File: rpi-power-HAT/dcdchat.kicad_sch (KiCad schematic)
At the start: 28 parts

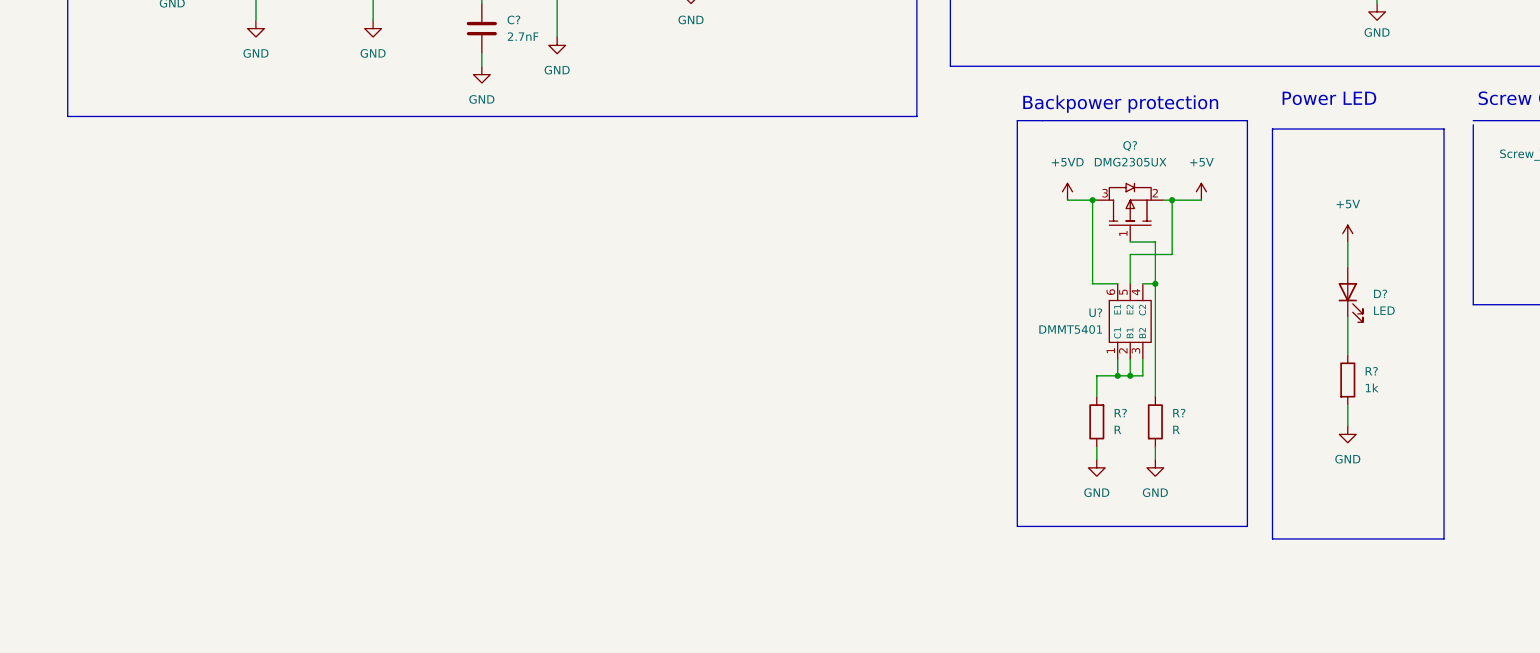
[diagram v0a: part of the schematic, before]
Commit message: added gpio connector
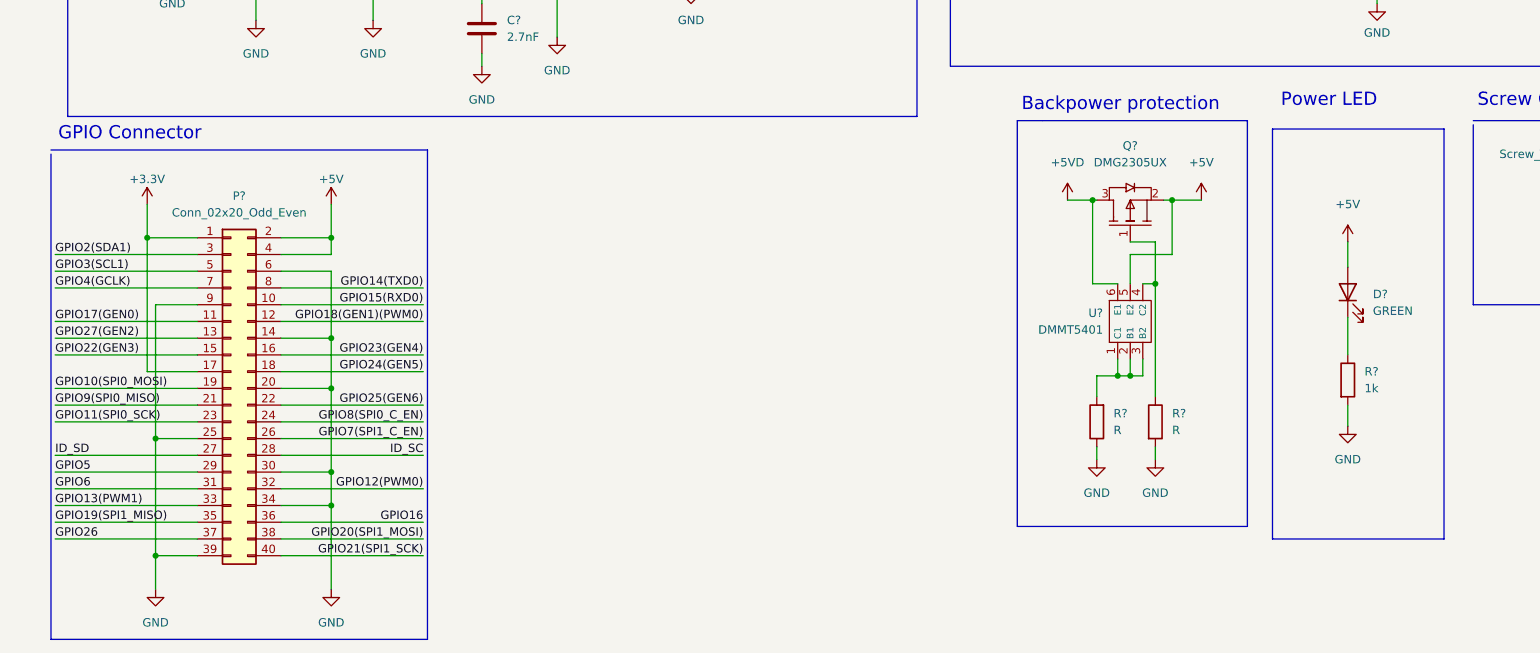
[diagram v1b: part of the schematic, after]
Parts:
- added P?: Conn_02x20_Odd_Even, Connector_PinSocket_2.54mm:PinSocket_2x20_P2.54mm_Vertical, symbol Library:Conn_02x20_Odd_Even
- D?: value LED -> GREEN
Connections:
- net +3.3V: now also P?.1 (Pin_1), P?.17 (Pin_17)
- net +5V: now also P?.2 (Pin_2), P?.4 (Pin_4)
- net GND: now also P?.14 (Pin_14), P?.20 (Pin_20), P?.25 (Pin_25), P?.30 (Pin_30), P?.34 (Pin_34), P?.39 (Pin_39), P?.6 (Pin_6), P?.9 (Pin_9)
- new net GPIO10(SPI0_MOSI): P?.19 (Pin_19)
- new net GPIO11(SPI0_SCK): P?.23 (Pin_23)
- new net GPIO12(PWM0): P?.32 (Pin_32)
- new net GPIO13(PWM1): P?.33 (Pin_33)
- new net GPIO14(TXD0): P?.8 (Pin_8)
- new net GPIO15(RXD0): P?.10 (Pin_10)
- new net GPIO16: P?.36 (Pin_36)
- new net GPIO17(GEN0): P?.11 (Pin_11)
- new net GPIO18(GEN1)(PWM0): P?.12 (Pin_12)
- new net GPIO19(SPI1_MISO): P?.35 (Pin_35)
- new net GPIO2(SDA1): P?.3 (Pin_3)
- new net GPIO20(SPI1_MOSI): P?.38 (Pin_38)
- new net GPIO21(SPI1_SCK): P?.40 (Pin_40)
- new net GPIO22(GEN3): P?.15 (Pin_15)
- new net GPIO23(GEN4): P?.16 (Pin_16)
- new net GPIO24(GEN5): P?.18 (Pin_18)
- new net GPIO25(GEN6): P?.22 (Pin_22)
- new net GPIO26: P?.37 (Pin_37)
- new net GPIO27(GEN2): P?.13 (Pin_13)
- new net GPIO3(SCL1): P?.5 (Pin_5)
- new net GPIO4(GCLK): P?.7 (Pin_7)
- new net GPIO5: P?.29 (Pin_29)
- new net GPIO6: P?.31 (Pin_31)
- new net GPIO7(SPI1_C_EN): P?.26 (Pin_26)
- new net GPIO8(SPI0_C_EN): P?.24 (Pin_24)
- new net GPIO9(SPI0_MISO): P?.21 (Pin_21)
- new net ID_SC: P?.28 (Pin_28)
- new net ID_SD: P?.27 (Pin_27)
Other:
- note added: "GPIO Connector"

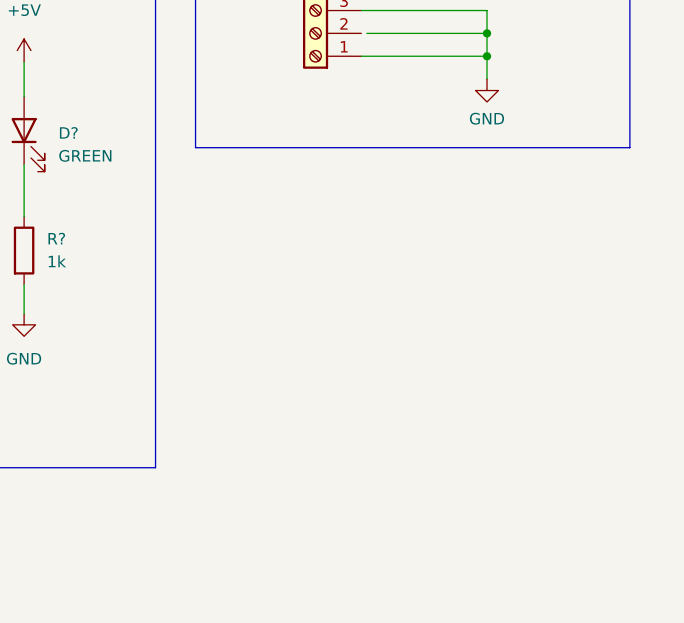
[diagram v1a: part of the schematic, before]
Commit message: Added readme, added CHassis connector
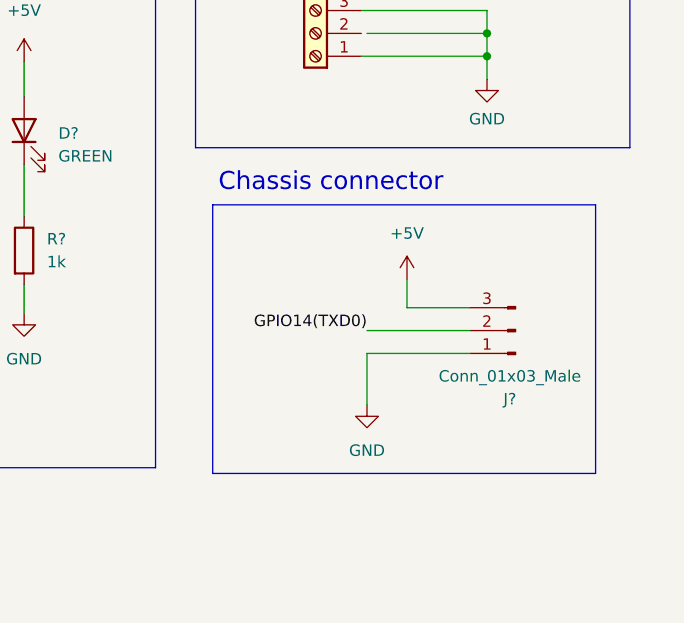
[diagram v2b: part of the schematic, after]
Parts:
- added J?: Conn_01x03_Male, symbol Connector:Conn_01x03_Male
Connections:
- net +5V: now also J?.3 (Pin_3)
- net GND: now also J?.1 (Pin_1)
- net GPIO14(TXD0): now also J?.2 (Pin_2)
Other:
- note added: "Chassis connector"
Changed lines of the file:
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@@
+    (stroke (width 0) (type default) (color 0 0 0 0))
+  )
+  (wire (pts (xy 248.92 131.445) (xy 260.35 131.445))
     (stroke (width 0) (type default) (color 0 0 0 0))
   )
@@
     (stroke (width 0) (type default) (color 0 0 0 0))
   )
+  (polyline (pts (xy 231.775 117.475) (xy 231.775 147.32))
+    (stroke (width 0) (type default) (color 0 0 0 0))
+  )
   (wire (pts (xy 215.265 36.83) (xy 215.265 40.005))
     (stroke (width 0) (type default) (color 0 0 0 0))
@@
     (stroke (width 0) (type default) (color 0 0 0 0))
   )
+  (polyline (pts (xy 231.775 117.475) (xy 274.32 117.475))
+    (stroke (width 0) (type default) (color 0 0 0 0))
+  )
   (wire (pts (xy 248.92 98.425) (xy 262.255 98.425))
     (stroke (width 0) (type default) (color 0 0 0 0))
@@
     (stroke (width 0) (type default) (color 0 0 0 0))
   )
+  (wire (pts (xy 253.365 125.73) (xy 253.365 128.905))
+    (stroke (width 0) (type default) (color 0 0 0 0))
+  )
   (polyline (pts (xy 150.495 17.145) (xy 150.495 74.93))
     (stroke (width 0) (type default) (color 0 0 0 0))
@@
     (stroke (width 0) (type default) (color 0 0 0 0))
   )
+  (polyline (pts (xy 274.32 117.475) (xy 274.32 147.32))
+    (stroke (width 0) (type default) (color 0 0 0 0))
+  )
   (wire (pts (xy 51.435 52.705) (xy 45.085 52.705))
     (stroke (width 0) (type default) (color 0 0 0 0))
@@
     (stroke (width 0) (type default) (color 0 0 0 0))
   )
+  (polyline (pts (xy 274.32 147.32) (xy 231.775 147.32))
+    (stroke (width 0) (type default) (color 0 0 0 0))
+  )
   (wire (pts (xy 172.72 132.715) (xy 172.72 134.62))
     (stroke (width 0) (type default) (color 0 0 0 0))
@@
     (stroke (width 0) (type default) (color 0 0 0 0))
   )
+  (wire (pts (xy 260.35 128.905) (xy 253.365 128.905))
+    (stroke (width 0) (type default) (color 0 0 0 0))
+  )
   (wire (pts (xy 48.895 128.905) (xy 70.485 128.905))
     (stroke (width 0) (type default) (color 0 0 0 0))
@@
     (stroke (width 0) (type default) (color 0 0 0 0))
   )
+  (wire (pts (xy 260.35 133.985) (xy 248.92 133.985))
+    (stroke (width 0) (type default) (color 0 0 0 0))
+  )
   (wire (pts (xy 28.575 121.285) (xy 36.195 121.285))
     (stroke (width 0) (type default) (color 0 0 0 0))
@@
   )
   (polyline (pts (xy 195.58 83.185) (xy 195.58 144.78))
+    (stroke (width 0) (type default) (color 0 0 0 0))
+  )
+  (wire (pts (xy 248.92 133.985) (xy 248.92 139.7))
     (stroke (width 0) (type default) (color 0 0 0 0))
   )
@@
     (effects (font (size 2 2)) (justify left bottom))
   )
+  (text "Chassis connector" (at 232.41 116.205 0)
+    (effects (font (size 2 2)) (justify left bottom))
+  )
   (text "Power LED" (at 200.66 81.28 0)
     (effects (font (size 2 2)) (justify left bottom))
@@
   )
   (label "GPIO20(SPI1_MOSI)" (at 70.485 146.685 180)
+    (effects (font (size 1.27 1.27)) (justify right bottom))
+  )
+  (label "GPIO14(TXD0)" (at 248.92 131.445 180)
     (effects (font (size 1.27 1.27)) (justify right bottom))
   )
@@
     )
     (property "Datasheet" "" (id 3) (at 262.255 90.805 0)
+      (effects (font (size 1.27 1.27)) hide)
+    )
+    (pin "1")
+  )
+  (symbol (lib_id "power:GND") (at 248.92 139.7 0) (unit 1)
+    (in_bom yes) (on_board yes) (fields_autoplaced)
+    (property "Reference" "#PWR?" (id 0) (at 248.92 146.05 0)
+      (effects (font (size 1.27 1.27)) hide)
+    )
+    (property "Value" "GND" (id 1) (at 248.92 144.78 0))
+    (property "Footprint" "" (id 2) (at 248.92 139.7 0)
+      (effects (font (size 1.27 1.27)) hide)
+    )
+    (property "Datasheet" "" (id 3) (at 248.92 139.7 0)
       (effects (font (size 1.27 1.27)) hide)
     )
@@
     (pin "4")
     (pin "5")
+  )
+  (symbol (lib_id "Connector:Conn_01x03_Male") (at 265.43 131.445 180) (unit 1)
+    (in_bom yes) (on_board yes) (fields_autoplaced)
+    (property "Reference" "J?" (id 0) (at 264.795 139.065 0))
+    (property "Value" "Conn_01x03_Male" (id 1) (at 264.795 136.525 0))
+    (property "Footprint" "" (id 2) (at 265.43 131.445 0)
+      (effects (font (size 1.27 1.27)) hide)
+    )
+    (property "Datasheet" "~" (id 3) (at 265.43 131.445 0)
+      (effects (font (size 1.27 1.27)) hide)
+    )
+    (pin "1")
+    (pin "2")
+    (pin "3")
   )
   (symbol (lib_id "power:GND") (at 181.61 134.62 0) (unit 1)
@@
     (pin "1")
   )
+  (symbol (lib_id "power:+5V") (at 253.365 125.73 0) (unit 1)
+    (in_bom yes) (on_board yes) (fields_autoplaced)
+    (property "Reference" "#PWR?" (id 0) (at 253.365 129.54 0)
+      (effects (font (size 1.27 1.27)) hide)
+    )
+    (property "Value" "+5V" (id 1) (at 253.365 120.65 0))
+    (property "Footprint" "" (id 2) (at 253.365 125.73 0)
+      (effects (font (size 1.27 1.27)) hide)
+    )
+    (property "Datasheet" "" (id 3) (at 253.365 125.73 0)
+      (effects (font (size 1.27 1.27)) hide)
+    )
+    (pin "1")
+  )
   (symbol (lib_id "Device:R") (at 210.82 122.555 0) (unit 1)
     (in_bom yes) (on_board yes) (fields_autoplaced)
@@
       (reference "#PWR?") (unit 1) (value "VCC") (footprint "")
     )
+    (path "/1683b790-0de4-48f6-98f7-032bf4ffe128"
+      (reference "#PWR?") (unit 1) (value "GND") (footprint "")
+    )
     (path "/16c81207-e246-4f87-8952-3ebeb878f8cb"
       (reference "#PWR?") (unit 1) (value "GND") (footprint "")
@@
       (reference "#PWR?") (unit 1) (value "+5VD") (footprint "")
     )
+    (path "/dfc07625-ddae-4ee3-aa1d-cab8d3a957a5"
+      (reference "#PWR?") (unit 1) (value "+5V") (footprint "")
+    )
     (path "/e69f3ab5-0847-439a-88e5-85d6eccfddba"
       (reference "#PWR?") (unit 1) (value "GND") (footprint "")
@@
       (reference "J?") (unit 1) (value "Screw_Terminal_01x05") (footprint "")
     )
+    (path "/739f876b-99d3-497e-b99f-98cc80035177"
+      (reference "J?") (unit 1) (value "Conn_01x03_Male") (footprint "")
+    )
     (path "/3eb396dd-1ed2-4bf1-bdc4-46cd0052b75b"

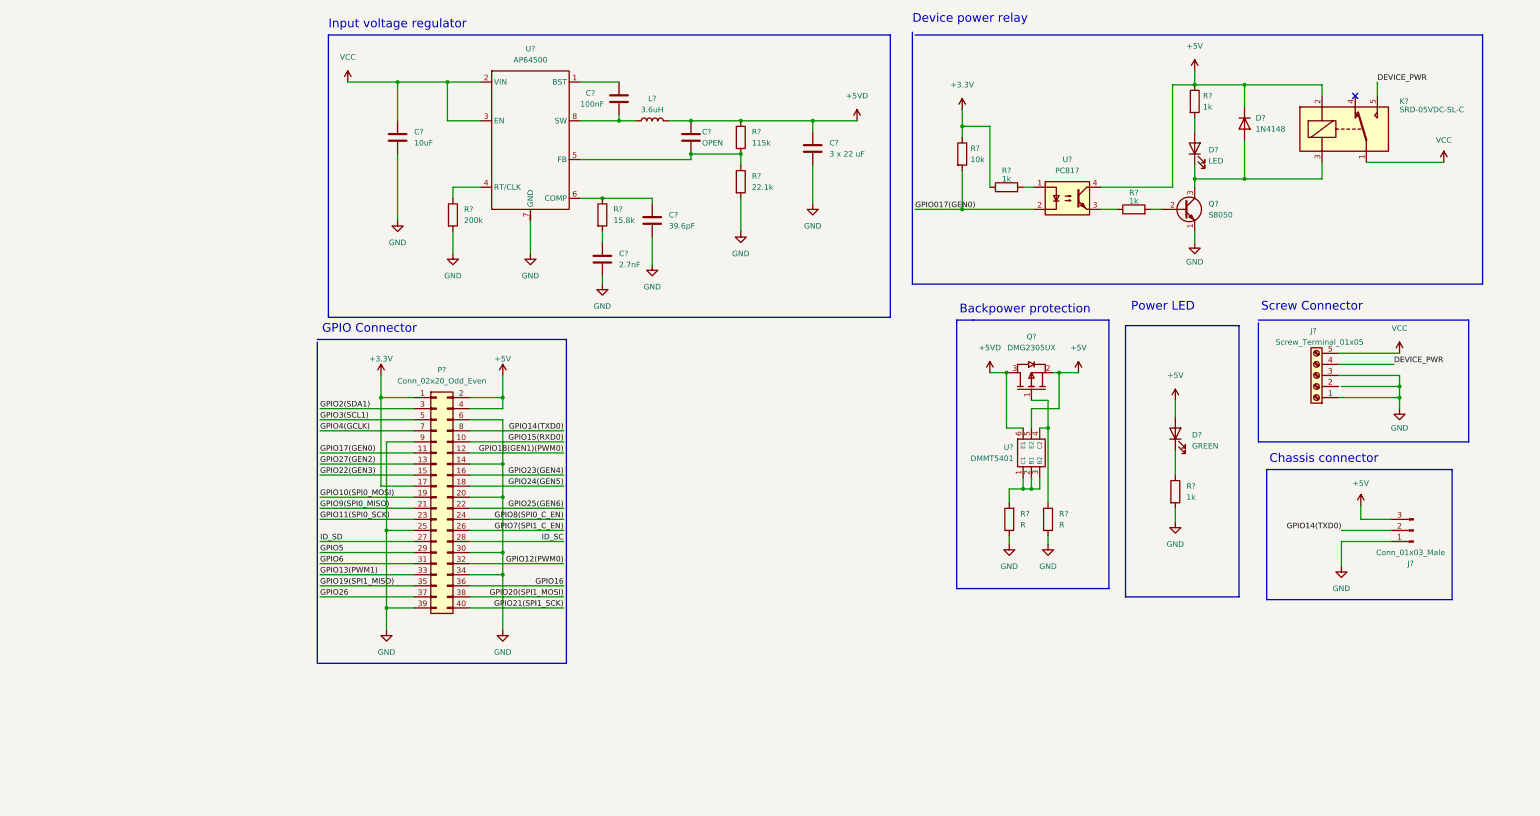
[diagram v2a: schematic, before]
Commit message: Fixes in pinout, deleting relay
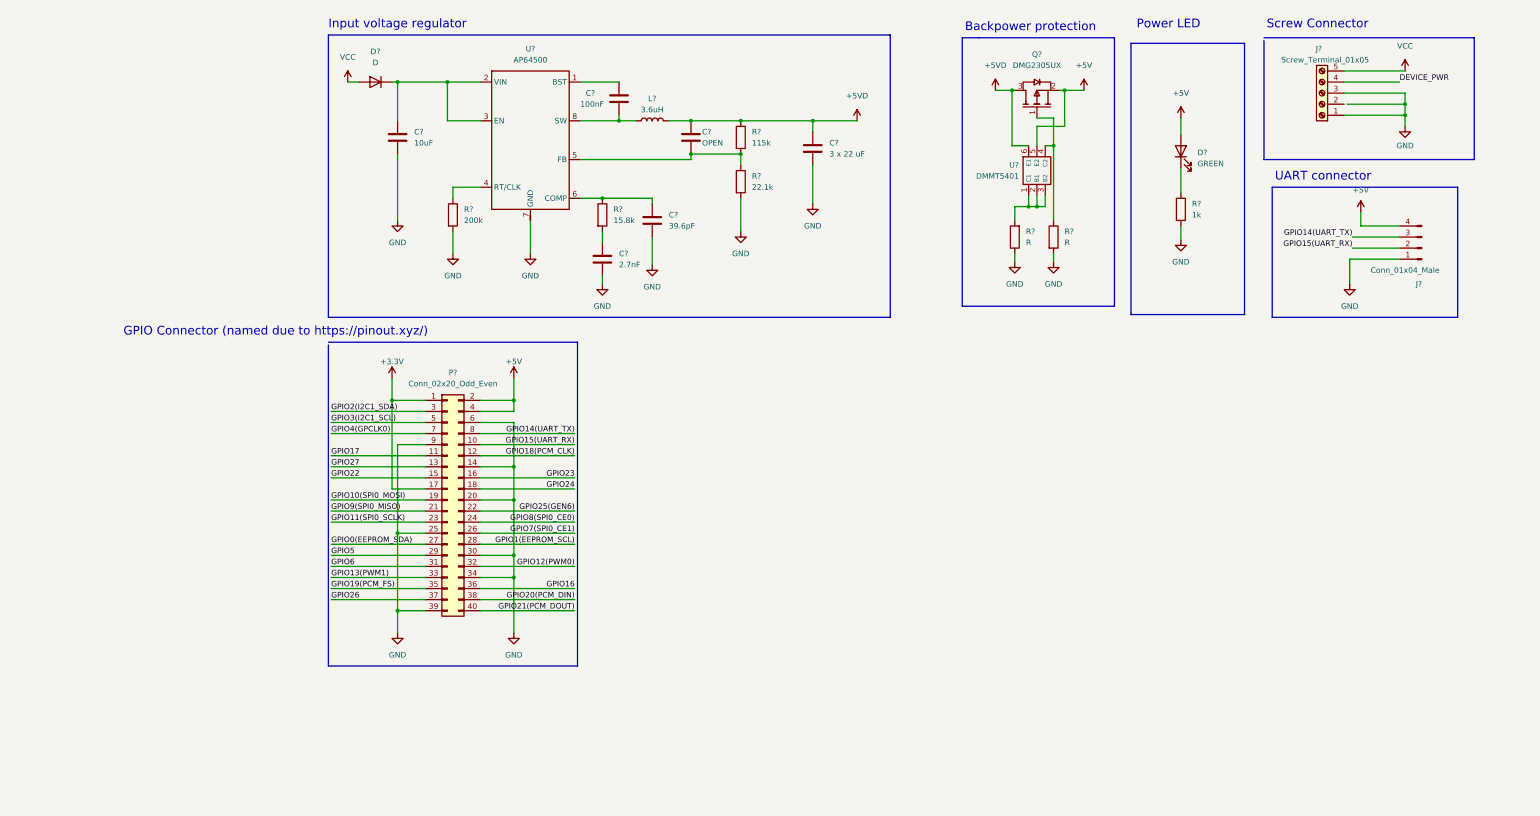
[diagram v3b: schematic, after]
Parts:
- removed D?: LED, symbol Device:LED
- removed D?: 1N4148, Diode_THT:D_DO-35_SOD27_P7.62mm_Horizontal, symbol Diode:1N4148
- removed J?: Conn_01x03_Male, symbol Connector:Conn_01x03_Male
- removed K?: SRD-05VDC-SL-C, SRD, symbol Library:SRD-05VDC-SL-C
- removed Q?: S8050, Package_TO_SOT_THT:TO-92_Inline, symbol Transistor_BJT:S8050
- removed R? (x3): 1k, symbol Device:R
- removed R?: 10k, symbol Device:R
- removed U?: PC817, Package_DIP:DIP-4_W7.62mm, symbol Isolator:PC817
- added D?: D, symbol Device:D
- added J?: Conn_01x04_Male, symbol Connector:Conn_01x04_Male
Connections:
- net +5V: now also J?.4 (Pin_4)
- net GND: now also J?.1 (Pin_1)
- net VCC: now also D?.2 (A); no longer C?.1, U?.2 (VIN), U?.3 (EN)
- net GPIO11(SPI0_SCK) renamed GPIO11(SPI0_SCLK)
- net GPIO14(TXD0) renamed GPIO14(UART_TX)
- net GPIO14(UART_TX): now also J?.3 (Pin_3)
- net GPIO15(RXD0) renamed GPIO15(UART_RX)
- net GPIO15(UART_RX): now also J?.2 (Pin_2)
- net GPIO17(GEN0) renamed GPIO17
- net GPIO18(GEN1)(PWM0) renamed GPIO18(PCM_CLK)
- net GPIO19(SPI1_MISO) renamed GPIO19(PCM_FS)
- net GPIO2(SDA1) renamed GPIO2(I2C1_SDA)
- net GPIO20(SPI1_MOSI) renamed GPIO20(PCM_DIN)
- net GPIO21(SPI1_SCK) renamed GPIO21(PCM_DOUT)
- net GPIO22(GEN3) renamed GPIO22
- net GPIO23(GEN4) renamed GPIO23
- net GPIO24(GEN5) renamed GPIO24
- net GPIO27(GEN2) renamed GPIO27
- net GPIO3(SCL1) renamed GPIO3(I2C1_SCL)
- net GPIO4(GCLK) renamed GPIO4(GPCLK0)
- net GPIO7(SPI1_C_EN) renamed GPIO7(SPI0_CE1)
- net GPIO8(SPI0_C_EN) renamed GPIO8(SPI0_CE0)
- net ID_SC renamed GPIO1(EEPROM_SCL)
- net ID_SD renamed GPIO0(EEPROM_SDA)
- new net: C?.1, D?.1 (K), U?.2 (VIN), U?.3 (EN)
- no-connect marks 1 -> 0
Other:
- note added: "GPIO Connector (named due to https://pinout.xyz/)"
- note added: "UART connector"
- note removed: "Chassis connector"
- note removed: "Device power relay"
- note removed: "GPIO Connector"
- moved on the sheet: D?, J?, P?, Q?, R?, U?
